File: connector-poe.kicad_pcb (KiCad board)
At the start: 4 copper layers, 73.5 x 20 mm, 42 parts, among them J101 2x05_Horizontal, J102 NE8FAH, J103 JAE_DX07S016JA3, J104 2x05_Horizontal, J105 NE8FAH, J106 WAGO-2065, J107 WAGO-2065, J108 WAGO-2065, J109 WAGO-2065, Q201 BSC010N04LS, U201 LM74502-Q1, U301 TPSM33625

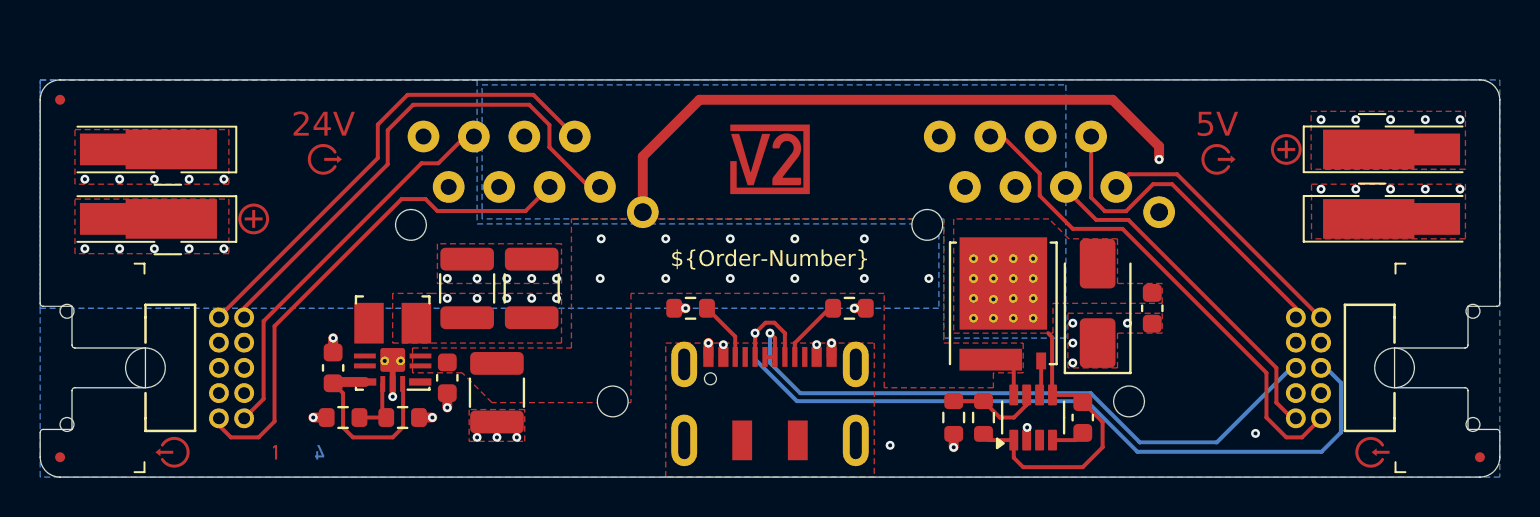
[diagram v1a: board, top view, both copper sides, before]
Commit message: Back-to-back Mosfet
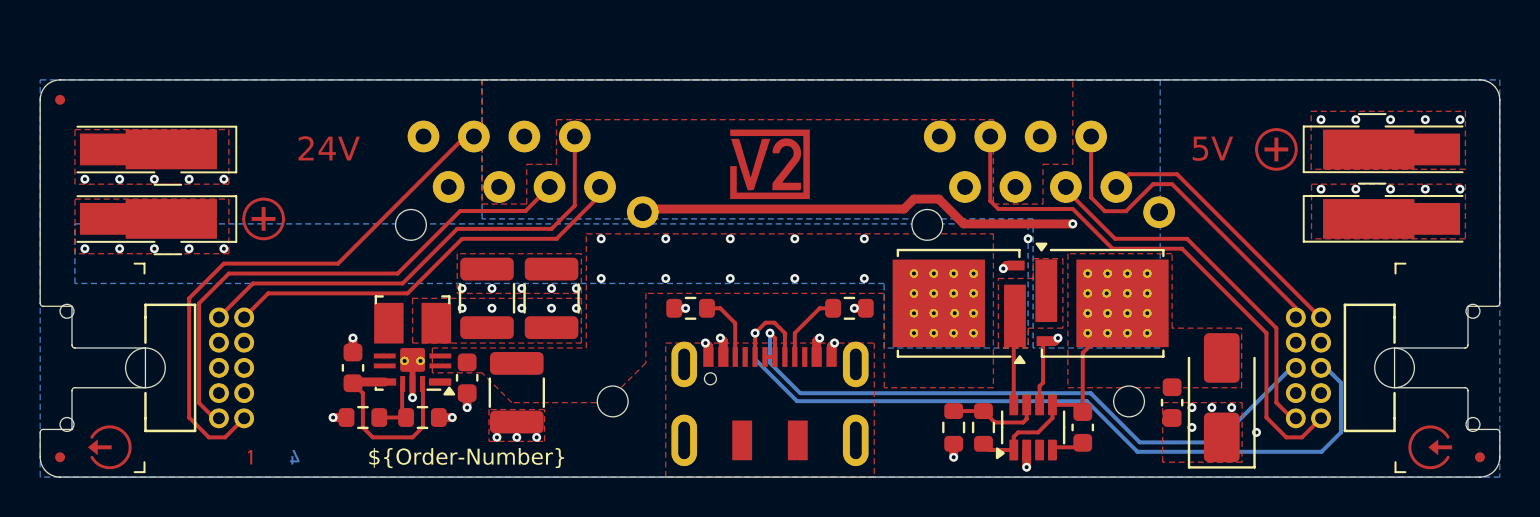
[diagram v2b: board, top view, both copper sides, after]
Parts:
- removed ICON110, ICON111: Arrow_Out, V2_Artwork:Arrow_Out
- added Q301: BSC010N04LS, V2_Package_TO_SOT_SMD:TDSON-8-FL, F.Cu at (163.2, 106.2)
- R202: value 4k7 -> 3k9
- moved INFO102 18.2 mm to (138.5, 114.0)
- moved TVS101 7.85 mm to (176.5, 111.0)
- moved Q201 5.00 mm to (170.5, 106.2), turned to 0 degrees
- moved C102 4.85 mm to (174.0, 111.2)
- moved ICON104 3.26 mm to (120.5, 113.5)
- moved ICON101 3.01 mm to (187.0, 113.5)
- moved ICON106 1.27 mm to (176.0, 98.5)
- moved ICON107 1.27 mm to (131.5, 98.5)
- moved INFO101 1.27 mm to (128.8, 114.0)
- moved C303 1.12 mm to (142.8, 106.0)
- moved C304 1.12 mm to (139.5, 106.0)
- moved C301 1.00 mm to (141.0, 110.8)
- moved C302 1.00 mm to (138.5, 110.0)
- moved C305 1.00 mm to (132.8, 109.5)
- moved R301 1.00 mm to (133.2, 112.0)
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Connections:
- C102 pad 1: /+24V-Input -> /+24V-Supply
- C201 pad 1: /+24V-Input -> /+24V-Supply
- C301 pad 1: /+24V-Supply -> +24V
- C302 pad 1: /+24V-Supply -> +24V
- J102 pad 4: /+24V-Input -> /+24V-Supply
- J102 pad 5: /+24V-Input -> /+24V-Supply
- J105 pad 4: /+24V-Input -> /+24V-Supply
- J105 pad 5: /+24V-Input -> /+24V-Supply
- J106 pad 1: /+24V-Supply -> +24V
- Q201 pad 1: /+24V-Supply -> /Polarity Protection/Source
- Q201 pad 5: /+24V-Input -> /+24V-Supply
- R201 pad 1: /+24V-Input -> /+24V-Supply
- TVS101 pad 2: /+24V-Input -> /+24V-Supply
- U201 pad 1: /+24V-Input -> /+24V-Supply
- U201 pad 5: /+24V-Input -> /+24V-Supply
- U201 pad 8: /+24V-Supply -> /Polarity Protection/Source
- U301 pad 2: /+24V-Supply -> +24V
- U301 pad 3: /+24V-Supply -> +24V
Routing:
- net /+24V-Input: track 15.2 -> 0.00 mm
- net /+24V-Supply: track 3.19 -> 12.8 mm, vias 16 -> 0
- net /Socket-TX-Z: track 19.7 -> 27.3 mm
- net /Polarity Protection/Gate: track 2.00 -> 9.39 mm, vias 0 -> 2
- net /RJ45-Shield: track 34.3 -> 27.2 mm
- net /Socket-RX-A: track 26.0 -> 21.4 mm
- net /Polarity Protection/Source: track 0.00 -> 4.00 mm
- net /Plug-RX-B: track 25.3 -> 27.7 mm
- net VBUS: track 5.94 -> 7.23 mm
- net /Plug-RX-A: track 17.5 -> 18.7 mm
- net /Socket-RX-B: track 24.4 -> 23.8 mm
- net /Socket-TX-Y: track 25.8 -> 26.4 mm
- net +24V: vias 0 -> 15
- added copper zone on B.Cu, net +24V
- added copper zone on F.Cu, net +24V
- added copper zone on In2.Cu, net +24V
- added copper zone on In2.Cu, net /+24V-Supply
- added copper zone on F.Cu, net /Polarity Protection/Source
- added copper zone on In2.Cu, net GND
- removed copper zone on B.Cu, net /+24V-Input
- removed copper zone on F.Cu, net /+24V-Input
- removed copper zone on In1.Cu, net /+24V-Input
- removed copper zone on In2.Cu, net /+24V-Input

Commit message: Resize to 70 mm
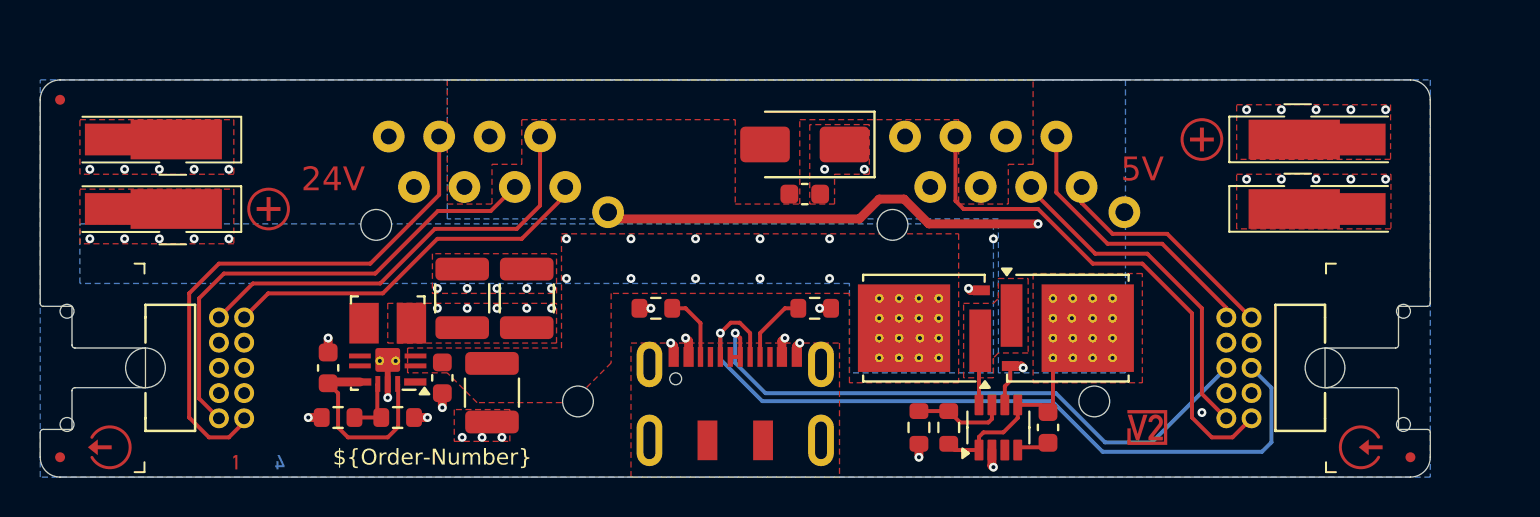
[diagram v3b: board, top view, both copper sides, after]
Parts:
- ICON102: footprint V2_Artwork:Logo_Small -> V2_Artwork:Logo_Tiny
- moved TVS101 24.6 mm to (155.5, 98.2), turned to 180 degrees
- moved ICON102 23.2 mm to (172.8, 112.5)
- moved C101 21.3 mm to (155.5, 100.8), turned to 0 degrees
- moved ICON103 3.78 mm to (175.5, 98.0)
- moved J107 3.78 mm to (180.8, 98.0)
- moved J108 3.78 mm to (180.8, 101.5)
- moved ICON101 3.64 mm to (172.5, 99.5)
- moved FID103 3.50 mm to (186.0, 114.0)
- moved ICON106 3.50 mm to (183.5, 113.5)
- moved J101 3.50 mm to (178.0, 109.5)
- moved PLUG101 3.50 mm to (178.0, 109.5)
- moved Q301 2.15 mm to (168.8, 107.5)
- moved Q302 2.15 mm to (161.5, 107.5)
- moved C301 1.75 mm to (167.8, 112.5)
- moved INFO102 1.75 mm to (136.8, 114.0)
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- renumbered C102 to C101, C201 to C301, C301 to C501, C302 to C502, C303 to C503, C304 to C504, C305 to C505, ICON106 to ICON101, ICON107 to ICON104, ICON101 to ICON106, ICON104 to ICON107, J108 to J107, J107 to J108, Q201 to Q301, Q301 to Q302, R201 to R301, R202 to R302, R301 to R501, R302 to R502, U201 to U301, U301 to U501
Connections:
- net /RJ45-Shield renamed /Shield
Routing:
- net /Plug-TX-Z: track 17.3 -> 14.3 mm
- net /+24V-Supply: track 12.8 -> 10.1 mm
- net /Plug-TX-Y: track 13.6 -> 11.8 mm
- net /Socket-RX-B: track 23.8 -> 22.0 mm
- net /USB+: track 33.0 -> 31.2 mm
- net /Socket-RX-A: track 21.4 -> 19.7 mm
- net /Socket-TX-Y: track 26.4 -> 24.7 mm
- net /USB-: track 41.3 -> 39.7 mm
- net /Plug-RX-A: track 18.7 -> 17.3 mm
- net /Plug-RX-B: track 27.7 -> 26.6 mm
- net /Polarity Protection/Gate: track 9.39 -> 8.59 mm
- net /Polarity Protection/Source: track 4.00 -> 3.34 mm
- net GND: track 7.34 -> 7.37 mm, vias 34 -> 32
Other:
- board size 73.5 x 20 mm -> 70 x 20 mm

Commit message: GND label
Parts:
- moved ICON104 11.0 mm to (122.2, 94.5)
- moved ICON101 10.6 mm to (181.8, 94.2)
- moved FID102 2.00 mm to (118.0, 94.0)
- moved ICON103 1.06 mm to (176.2, 97.2)
- moved ICON105 1.06 mm to (127.8, 100.8)
- moved J106 1.06 mm to (122.5, 100.8)
- moved J107 1.06 mm to (181.5, 97.2)
- moved J108 1.06 mm to (181.5, 100.8)
- moved J109 1.06 mm to (122.5, 97.2)
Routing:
- net GND: vias 32 -> 33
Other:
- board size 70 x 20 mm -> 70 x 22 mm
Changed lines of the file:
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@@
 	(footprint "V2_Connector_WAGO:2065-100"
 		(layer "F.Cu")
-		(at 123.25 101.5)
+		(at 122.5 100.75)
 		(property "Reference" "J106"
 			(at 0.5 -1.7352 0)
@@
 	(footprint "V2_Artwork:Plus_Small"
 		(layer "F.Cu")
-		(at 128.5 101.5 90)
+		(at 127.75 100.75 90)
 		(property "Reference" "ICON105"
 			(at 0 -2.5 90)
@@
 	(footprint "V2_Artwork:24V"
 		(layer "F.Cu")
-		(at 131.75 100)
+		(at 122.25 94.5)
 		(property "Reference" "ICON104"
 			(at 0 -2.5 0)
@@
 	(footprint "V2_Artwork:5V"
 		(layer "F.Cu")
-		(at 172.5 99.5)
+		(at 181.75 94.25)
 		(property "Reference" "ICON101"
 			(at 0 -2.5 0)
@@
 	(footprint "V2_Connector_WAGO:2065-100"
 		(layer "F.Cu")
-		(at 123.25 98)
+		(at 122.5 97.25)
 		(property "Reference" "J109"
 			(at 0.5 -1.7352 0)
@@
 	(footprint "V2_Connector_WAGO:2065-100"
 		(layer "F.Cu")
-		(at 180.75 98 180)
+		(at 181.5 97.25 180)
 		(property "Reference" "J107"
 			(at 0.5 -1.7352 0)
@@
 	(footprint "V2_Connector_WAGO:2065-100"
 		(layer "F.Cu")
-		(at 180.75 101.5 180)
+		(at 181.5 100.75 180)
 		(property "Reference" "J108"
 			(at 0.5 -1.7352 0)
@@
 	(footprint "V2_Fiducial:Fiducial_0.5mm_Mask1mm_Paste"
 		(layer "F.Cu")
-		(at 118 96)
+		(at 118 94)
 		(descr "Circular Fiducial, 0.5mm bare copper, 1mm soldermask opening (Level C)")
 		(tags "fiducial")
@@
 	(footprint "V2_Artwork:Plus_Small"
 		(layer "F.Cu")
-		(at 175.5 98 -90)
+		(at 176.25 97.25 -90)
 		(property "Reference" "ICON103"
 			(at 0 -2.5 270)
@@
 	)
 	(gr_line
-		(start 187 96)
+		(start 187 94)
 		(end 187 106.25)
 		(stroke
@@
 	)
 	(gr_line
-		(start 118 95)
-		(end 186 95)
+		(start 118 93)
+		(end 186 93)
 		(stroke
 			(width 0.05)
@@
 	)
 	(gr_line
-		(start 117 96)
+		(start 117 94)
 		(end 117 106.25)
 		(stroke
@@
 	)
 	(gr_arc
-		(start 117 96)
-		(mid 117.292893 95.292893)
-		(end 118 95)
+		(start 117 94)
+		(mid 117.292893 93.292893)
+		(end 118 93)
 		(stroke
 			(width 0.05)
@@
 	)
 	(gr_arc
-		(start 186 95)
-		(mid 186.707107 95.292893)
-		(end 187 96)
+		(start 186 93)
+		(mid 186.707107 93.292893)
+		(end 187 94)
 		(stroke
 			(width 0.05)
@@
 	)
 	(via
-		(at 179.5 100)
+		(at 180.25 99.25)
 		(size 0.45)
 		(drill 0.2)
@@
 	)
 	(via
-		(at 123 99.5)
+		(at 122.25 98.75)
 		(size 0.45)
 		(drill 0.2)
@@
 	)
 	(via
+		(at 182.25 114.5)
+		(size 0.45)
+		(drill 0.2)
+		(layers "F.Cu" "B.Cu")
+		(remove_unused_layers yes)
+		(keep_end_layers yes)
+		(free yes)
+		(zone_layer_connections "In1.Cu" "In2.Cu")
+		(net 1)
+	)
+	(via
 		(at 136.5 112)
 		(size 0.45)
@@
 	)
 	(via
-		(at 126.5 99.5)
+		(at 125.75 98.75)
 		(size 0.45)
 		(drill 0.2)
@@
 	)
 	(via
-		(at 119.5 99.5)
+		(at 118.75 98.75)
 		(size 0.45)
 		(drill 0.2)
@@
 	)
 	(via
-		(at 184.75 100)
+		(at 185.5 99.25)
 		(size 0.45)
 		(drill 0.2)
@@
 	)
 	(via
-		(at 183 100)
+		(at 183.75 99.25)
 		(size 0.45)
 		(drill 0.2)
@@
 	)
 	(via
-		(at 124.75 99.5)
+		(at 124 98.75)
 		(size 0.45)
 		(drill 0.2)
@@
 	)
 	(via
-		(at 181.25 100)
+		(at 182 99.25)
 		(size 0.45)
 		(drill 0.2)
@@
 		(keep_end_layers yes)
 		(free yes)
-		(zone_layer_connections "In1.Cu")
+		(zone_layer_connections "In1.Cu" "In2.Cu")
 		(net 1)
 	)
@@
 	)
 	(via
-		(at 121.25 99.5)
+		(at 120.5 98.75)
 		(size 0.45)
 		(drill 0.2)
@@
 	)
 	(via
-		(at 177.75 100)
+		(at 178.5 99.25)
 		(size 0.45)
 		(drill 0.2)
@@
 	)
 	(via
-		(at 179.5 96.5)
+		(at 180.25 95.75)
 		(size 0.45)
 		(drill 0.2)
@@
 	)
 	(via
-		(at 183 96.5)
+		(at 183.75 95.75)
 		(size 0.45)
 		(drill 0.2)
@@
 	)
 	(via
-		(at 184.75 96.5)
+		(at 185.5 95.75)
 		(size 0.45)
 		(drill 0.2)
@@
 	)
 	(via
-		(at 181.25 96.5)
+		(at 182 95.75)
 		(size 0.45)
 		(drill 0.2)
@@
 	)
 	(via
-		(at 177.75 96.5)
+		(at 178.5 95.75)
 		(size 0.45)
 		(drill 0.2)
@@
 	)
 	(via
-		(at 121.25 103)
+		(at 120.5 102.25)
 		(size 0.45)
 		(drill 0.2)
@@
 	)
 	(via
-		(at 119.5 103)
+		(at 118.75 102.25)
 		(size 0.45)
 		(drill 0.2)
@@
 	)
 	(via
-		(at 126.5 103)
+		(at 125.75 102.25)
 		(size 0.45)
 		(drill 0.2)
@@
 	)
 	(via
-		(at 124.75 103)
+		(at 124 102.25)
 		(size 0.45)
 		(drill 0.2)
@@
 	)
 	(via
-		(at 123 103)
+		(at 122.25 102.25)
 		(size 0.45)
 		(drill 0.2)
@@
 		(polygon
 			(pts
-				(xy 177.25 99) (xy 177.25 96.25) (xy 185 96.25) (xy 185 99)
+				(xy 177.5 98.5) (xy 177.5 95.5) (xy 186 95.5) (xy 186 98.5)
 			)
 		)
@@
 		(polygon
 			(pts
-				(xy 137.5 95) (xy 137.5 101.25) (xy 139.75 101.25) (xy 139.75 99.25) (xy 141.25 99.25) (xy 141.25 97)
+				(xy 137.5 93) (xy 137.5 101.25) (xy 139.75 101.25) (xy 139.75 99.25) (xy 141.25 99.25) (xy 141.25 97)
 				(xy 152 97) (xy 152 101.25) (xy 155.25 101.25) (xy 155.25 97) (xy 163.25 97) (xy 163.25 101.25)
-				(xy 165.75 101.25) (xy 165.75 99.25) (xy 167 99.25) (xy 167 95)
+				(xy 165.75 101.25) (xy 165.75 99.25) (xy 167 99.25) (xy 167 93)
 			)
 		)
@@
 		(polygon
 			(pts
-				(xy 177.25 102.5) (xy 177.25 99.75) (xy 185.02 99.75) (xy 185.02 102.5)
+				(xy 177.5 102) (xy 177.5 99) (xy 186 99) (xy 186 102)
 			)
 		)
@@
 		(polygon
 			(pts
-				(xy 126.75 100.5) (xy 126.75 103.25) (xy 119 103.25) (xy 119 100.5)
+				(xy 126.5 99.5) (xy 126.5 102.5) (xy 118 102.5) (xy 118 99.5)
 			)
 		)
@@
 		(polygon
 			(pts
-				(xy 126.75 97) (xy 126.75 99.75) (xy 119 99.75) (xy 119 97)
+				(xy 126.5 96) (xy 126.5 99) (xy 118 99) (xy 118 96)
 			)
 		)
@@
 		(polygon
 			(pts
-				(xy 117 115) (xy 117 95) (xy 187 95) (xy 187 115)
+				(xy 117 115) (xy 117 93) (xy 187 93) (xy 187 115)
 			)
 		)
@@
 		(polygon
 			(pts
-				(xy 119 102.25) (xy 165 102.25) (xy 165 109.75) (xy 157.75 109.75) (xy 157.75 105.25) (xy 119 105.25)
+				(xy 118.25 102) (xy 165 102) (xy 165 109.75) (xy 157.75 109.75) (xy 157.75 105.25) (xy 118.25 105.25)
 			)
 		)
@@
 		(polygon
 			(pts
-				(xy 171.65 109.75) (xy 165.25 109.75) (xy 165.25 102) (xy 137.5 102) (xy 137.5 95) (xy 171.65 95)
+				(xy 171.65 109.75) (xy 165.25 109.75) (xy 165.25 102) (xy 137.5 102) (xy 137.5 93) (xy 171.65 93)
 			)
 		)
@@
 		(polygon
 			(pts
-				(xy 185 99.25) (xy 181.75 99.25) (xy 181.75 115) (xy 130.25 115) (xy 130.25 106.25) (xy 143 106.25)
-				(xy 143 110) (xy 177.25 110) (xy 177.25 96.25) (xy 185 96.25)
+				(xy 185.75 98.25) (xy 181.75 98.25) (xy 181.75 115) (xy 130.25 115) (xy 130.25 106.25) (xy 143 106.25)
+				(xy 143 110) (xy 177.25 110) (xy 177.25 95.5) (xy 185.75 95.5)
 			)
 		)
